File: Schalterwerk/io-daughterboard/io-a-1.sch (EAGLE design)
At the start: 34 parts, among them Q1 BSS123, Q2 BSS123, Q3 BSS123, Q4 BSS123, Q5 BSS123, Q6 BSS123, Q7 BSS123, Q8 BSS123, U1 74HC166, U2 74HC166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

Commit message: Completes board layout and routing for the daughterboard.
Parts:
- removed C2, C4: (no value), rcl:C-USC0805
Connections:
- net N$1 renamed QA
- net N$11 renamed PF
- net N$12 renamed PE
- net N$14 renamed PH
- net N$15 renamed PG
- net N$17 renamed PC
- net N$2 renamed QB
- net N$23 renamed PD
- net N$3 renamed QC
- net N$39 renamed PB
- net N$4 renamed QD
- net N$41 renamed PA
- net N$5 renamed QE
- net N$6 renamed QF
- net N$7 renamed QG
- net N$8 renamed QH
- net +12V: now also X1.6; no longer X1.1
- net +5V: no longer C2.1, C4.1
- net GND: now also X1.1; no longer C2.2, C4.2, X1.6
- net LATCH: now also X1.2; no longer X1.5
- net MISO-DN: now also X1.5; no longer X1.2
- net MOSI-DN: now also X1.4; no longer X1.3
- net SCK: now also X1.3; no longer X1.4
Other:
- moved on the sheet: C3, X1
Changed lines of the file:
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@@
 <part name="P+31" library="supply1" library_urn="urn:adsk.eagle:library:371" deviceset="+5V" device=""/>
 <part name="SJ2" library="trainlib" deviceset="SJ" device="RND2"/>
-<part name="C4" library="rcl" library_urn="urn:adsk.eagle:library:334" deviceset="C-US" device="C0805" package3d_urn="urn:adsk.eagle:package:23617/2"/>
-<part name="C2" library="rcl" library_urn="urn:adsk.eagle:library:334" deviceset="C-US" device="C0805" package3d_urn="urn:adsk.eagle:package:23617/2"/>
 <part name="U4" library="trainlib" deviceset="74*595" device="D" technology="HCT" value="74AHCT595N"/>
 <part name="SUPPLY4" library="supply2" library_urn="urn:adsk.eagle:library:372" deviceset="GND" device=""/>
@@
 <attribute name="VALUE" x="190.5" y="161.925" size="1.778" layer="96" rot="MR0"/>
 </instance>
-<instance part="X1" gate="G$1" x="236.22" y="170.18" smashed="yes" rot="R270">
-<attribute name="NAME" x="236.22" y="179.07" size="1.778" layer="95"/>
-<attribute name="VALUE" x="236.22" y="161.925" size="1.778" layer="96"/>
+<instance part="X1" gate="G$1" x="236.22" y="172.72" smashed="yes" rot="MR90">
+<attribute name="NAME" x="236.22" y="163.83" size="1.778" layer="95" rot="MR180"/>
+<attribute name="VALUE" x="236.22" y="180.975" size="1.778" layer="96" rot="MR180"/>
 </instance>
 <instance part="P+4" gate="1" x="200.66" y="182.88" smashed="yes">
@@
 <attribute name="VALUE" x="26.67" y="17.78" size="1.778" layer="96" rot="R90"/>
 </instance>
-<instance part="C4" gate="G$1" x="228.6" y="45.72" smashed="yes" rot="R90">
-<attribute name="NAME" x="232.156" y="46.355" size="1.778" layer="95"/>
-<attribute name="VALUE" x="232.791" y="46.736" size="1.778" layer="96" rot="R90"/>
-</instance>
 <instance part="U2" gate="P" x="228.6" y="83.82" smashed="yes" rot="MR270">
 <attribute name="NAME" x="226.187" y="85.725" size="1.778" layer="95" rot="MR180"/>
-</instance>
-<instance part="C2" gate="G$1" x="228.6" y="60.96" smashed="yes" rot="R90">
-<attribute name="NAME" x="232.156" y="61.595" size="1.778" layer="95"/>
-<attribute name="VALUE" x="232.791" y="61.976" size="1.778" layer="96" rot="R90"/>
 </instance>
 <instance part="U4" gate="A" x="106.68" y="35.56" smashed="yes" rot="MR0">
@@
 <attribute name="NAME" x="226.187" y="75.565" size="1.778" layer="95" rot="MR180"/>
 </instance>
-<instance part="C3" gate="G$1" x="228.6" y="53.34" smashed="yes" rot="MR270">
-<attribute name="NAME" x="231.902" y="55.753" size="1.778" layer="95" rot="MR180"/>
-<attribute name="VALUE" x="232.791" y="52.324" size="1.778" layer="96" rot="MR270"/>
-</instance>
-<instance part="SUPPLY6" gate="GND" x="241.3" y="40.64" smashed="yes" rot="MR0">
-<attribute name="VALUE" x="243.205" y="37.465" size="1.778" layer="96" rot="MR0"/>
+<instance part="C3" gate="G$1" x="228.6" y="60.96" smashed="yes" rot="MR270">
+<attribute name="NAME" x="231.902" y="63.373" size="1.778" layer="95" rot="MR180"/>
+<attribute name="VALUE" x="232.791" y="59.944" size="1.778" layer="96" rot="MR270"/>
+</instance>
+<instance part="SUPPLY6" gate="GND" x="241.3" y="53.34" smashed="yes" rot="MR0">
+<attribute name="VALUE" x="243.205" y="50.165" size="1.778" layer="96" rot="MR0"/>
 </instance>
 <instance part="R1" gate="G$1" x="55.88" y="149.86" smashed="yes" rot="R90">
@@
 </segment>
 <segment>
-<pinref part="X1" gate="G$1" pin="6"/>
-<wire x1="233.68" y1="165.1" x2="228.6" y2="165.1" width="0.1524" layer="91"/>
 <pinref part="SUPPLY2" gate="GND" pin="GND"/>
 <wire x1="228.6" y1="165.1" x2="228.6" y2="162.56" width="0.1524" layer="91"/>
+<pinref part="X1" gate="G$1" pin="1"/>
+<wire x1="228.6" y1="165.1" x2="233.68" y2="165.1" width="0.1524" layer="91"/>
 </segment>
 <segment>
@@
 <pinref part="C3" gate="G$1" pin="2"/>
 <pinref part="U3" gate="P" pin="GND"/>
-<pinref part="C4" gate="G$1" pin="2"/>
 <pinref part="U2" gate="P" pin="GND"/>
-<pinref part="C2" gate="G$1" pin="2"/>
 <pinref part="U1" gate="P" pin="GND"/>
 <pinref part="C1" gate="G$1" pin="2"/>
@@
 <wire x1="241.3" y1="73.66" x2="241.3" y2="68.58" width="0.1524" layer="91"/>
 <wire x1="241.3" y1="68.58" x2="241.3" y2="60.96" width="0.1524" layer="91"/>
-<wire x1="241.3" y1="60.96" x2="241.3" y2="53.34" width="0.1524" layer="91"/>
-<wire x1="241.3" y1="53.34" x2="241.3" y2="45.72" width="0.1524" layer="91"/>
-<wire x1="241.3" y1="45.72" x2="241.3" y2="43.18" width="0.1524" layer="91"/>
+<wire x1="241.3" y1="60.96" x2="241.3" y2="55.88" width="0.1524" layer="91"/>
 <wire x1="238.76" y1="83.82" x2="241.3" y2="83.82" width="0.1524" layer="91"/>
 <junction x="241.3" y="83.82"/>
@@
 <wire x1="233.68" y1="60.96" x2="241.3" y2="60.96" width="0.1524" layer="91"/>
 <junction x="241.3" y="60.96"/>
-<wire x1="233.68" y1="53.34" x2="241.3" y2="53.34" width="0.1524" layer="91"/>
-<junction x="241.3" y="53.34"/>
-<wire x1="233.68" y1="45.72" x2="241.3" y2="45.72" width="0.1524" layer="91"/>
-<junction x="241.3" y="45.72"/>
 </segment>
 <segment>
@@
 </segment>
 <segment>
-<wire x1="226.06" y1="175.26" x2="233.68" y2="175.26" width="0.1524" layer="91"/>
-<pinref part="X1" gate="G$1" pin="2"/>
 <label x="226.06" y="175.26" size="1.27" layer="95" rot="R180" xref="yes"/>
+<pinref part="X1" gate="G$1" pin="5"/>
+<wire x1="233.68" y1="175.26" x2="226.06" y2="175.26" width="0.1524" layer="91"/>
 </segment>
 </net>
@@
 </segment>
 <segment>
-<wire x1="233.68" y1="170.18" x2="226.06" y2="170.18" width="0.1524" layer="91"/>
 <label x="226.06" y="170.18" size="1.27" layer="95" rot="MR0" xref="yes"/>
-<pinref part="X1" gate="G$1" pin="4"/>
+<pinref part="X1" gate="G$1" pin="3"/>
+<wire x1="226.06" y1="170.18" x2="233.68" y2="170.18" width="0.1524" layer="91"/>
 </segment>
 <segment>
@@
 </segment>
 <segment>
-<wire x1="233.68" y1="167.64" x2="226.06" y2="167.64" width="0.1524" layer="91"/>
 <label x="226.06" y="167.64" size="1.27" layer="95" rot="MR0" xref="yes"/>
-<pinref part="X1" gate="G$1" pin="5"/>
+<pinref part="X1" gate="G$1" pin="2"/>
+<wire x1="226.06" y1="167.64" x2="233.68" y2="167.64" width="0.1524" layer="91"/>
 </segment>
 <segment>
@@
 </segment>
 </net>
-<net name="N$1" class="0">
+<net name="QA" class="0">
 <segment>
 <pinref part="U1" gate="A" pin="A"/>
@@
 </segment>
 </net>
-<net name="N$2" class="0">
+<net name="QB" class="0">
 <segment>
 <pinref part="U2" gate="A" pin="B"/>
@@
 </segment>
 </net>
-<net name="N$3" class="0">
+<net name="QC" class="0">
 <segment>
 <pinref part="U1" gate="A" pin="C"/>
@@
 </segment>
 </net>
-<net name="N$4" class="0">
+<net name="QD" class="0">
 <segment>
 <pinref part="U2" gate="A" pin="D"/>
@@
 </segment>
 </net>
-<net name="N$5" class="0">
+<net name="QE" class="0">
 <segment>
 <pinref part="U1" gate="A" pin="E"/>
@@
 </segment>
 </net>
-<net name="N$6" class="0">
+<net name="QF" class="0">
 <segment>
 <pinref part="U2" gate="A" pin="F"/>
@@
 </segment>
 </net>
-<net name="N$7" class="0">
+<net name="QG" class="0">
 <segment>
 <pinref part="U1" gate="A" pin="G"/>
@@
 </segment>
 </net>
-<net name="N$8" class="0">
+<net name="QH" class="0">
 <segment>
 <pinref part="U2" gate="A" pin="H"/>
@@
 <wire x1="215.9" y1="68.58" x2="226.06" y2="68.58" width="0.1524" layer="91"/>
 <junction x="215.9" y="73.66"/>
-<pinref part="C2" gate="G$1" pin="1"/>
+<junction x="215.9" y="68.58"/>
+<pinref part="C3" gate="G$1" pin="1"/>
 <wire x1="215.9" y1="68.58" x2="215.9" y2="60.96" width="0.1524" layer="91"/>
 <wire x1="215.9" y1="60.96" x2="226.06" y2="60.96" width="0.1524" layer="91"/>
-<junction x="215.9" y="68.58"/>
-<pinref part="C3" gate="G$1" pin="1"/>
-<wire x1="215.9" y1="60.96" x2="215.9" y2="53.34" width="0.1524" layer="91"/>
-<wire x1="215.9" y1="53.34" x2="226.06" y2="53.34" width="0.1524" layer="91"/>
-<junction x="215.9" y="60.96"/>
-<pinref part="C4" gate="G$1" pin="1"/>
-<wire x1="215.9" y1="53.34" x2="215.9" y2="45.72" width="0.1524" layer="91"/>
-<wire x1="215.9" y1="45.72" x2="226.06" y2="45.72" width="0.1524" layer="91"/>
-<junction x="215.9" y="53.34"/>
 </segment>
 <segment>
@@
 </segment>
 <segment>
-<pinref part="X1" gate="G$1" pin="1"/>
-<wire x1="233.68" y1="177.8" x2="228.6" y2="177.8" width="0.1524" layer="91"/>
 <pinref part="P+5" gate="1" pin="+12V"/>
 <wire x1="228.6" y1="177.8" x2="228.6" y2="180.34" width="0.1524" layer="91"/>
+<pinref part="X1" gate="G$1" pin="6"/>
+<wire x1="228.6" y1="177.8" x2="233.68" y2="177.8" width="0.1524" layer="91"/>
 </segment>
 <segment>
@@
 <net name="MOSI-DN" class="0">
 <segment>
-<pinref part="X1" gate="G$1" pin="3"/>
-<wire x1="233.68" y1="172.72" x2="226.06" y2="172.72" width="0.1524" layer="91"/>
 <label x="226.06" y="172.72" size="1.27" layer="95" rot="R180" xref="yes"/>
+<pinref part="X1" gate="G$1" pin="4"/>
+<wire x1="226.06" y1="172.72" x2="233.68" y2="172.72" width="0.1524" layer="91"/>
 </segment>
 <segment>
@@
 </segment>
 </net>
-<net name="N$12" class="0">
+<net name="PE" class="0">
 <segment>
 <pinref part="Q5" gate="G$1" pin="G"/>
@@
 </segment>
 </net>
-<net name="N$17" class="0">
+<net name="PC" class="0">
 <segment>
 <pinref part="Q3" gate="G$1" pin="G"/>
@@
 </segment>
 </net>
-<net name="N$39" class="0">
+<net name="PB" class="0">
 <segment>
 <pinref part="Q2" gate="G$1" pin="G"/>
@@
 </segment>
 </net>
-<net name="N$41" class="0">
+<net name="PA" class="0">
 <segment>
 <pinref part="Q1" gate="G$1" pin="G"/>
@@
 </segment>
 </net>
-<net name="N$11" class="0">
+<net name="PF" class="0">
 <segment>
 <pinref part="Q6" gate="G$1" pin="G"/>
@@
 </segment>
 </net>
-<net name="N$14" class="0">
+<net name="PH" class="0">
 <segment>
 <pinref part="Q8" gate="G$1" pin="G"/>
@@
 </segment>
 </net>
-<net name="N$15" class="0">
+<net name="PG" class="0">
 <segment>
 <pinref part="Q7" gate="G$1" pin="G"/>
@@
 </segment>
 </net>
-<net name="N$23" class="0">
+<net name="PD" class="0">
 <segment>
 <pinref part="Q4" gate="G$1" pin="G"/>

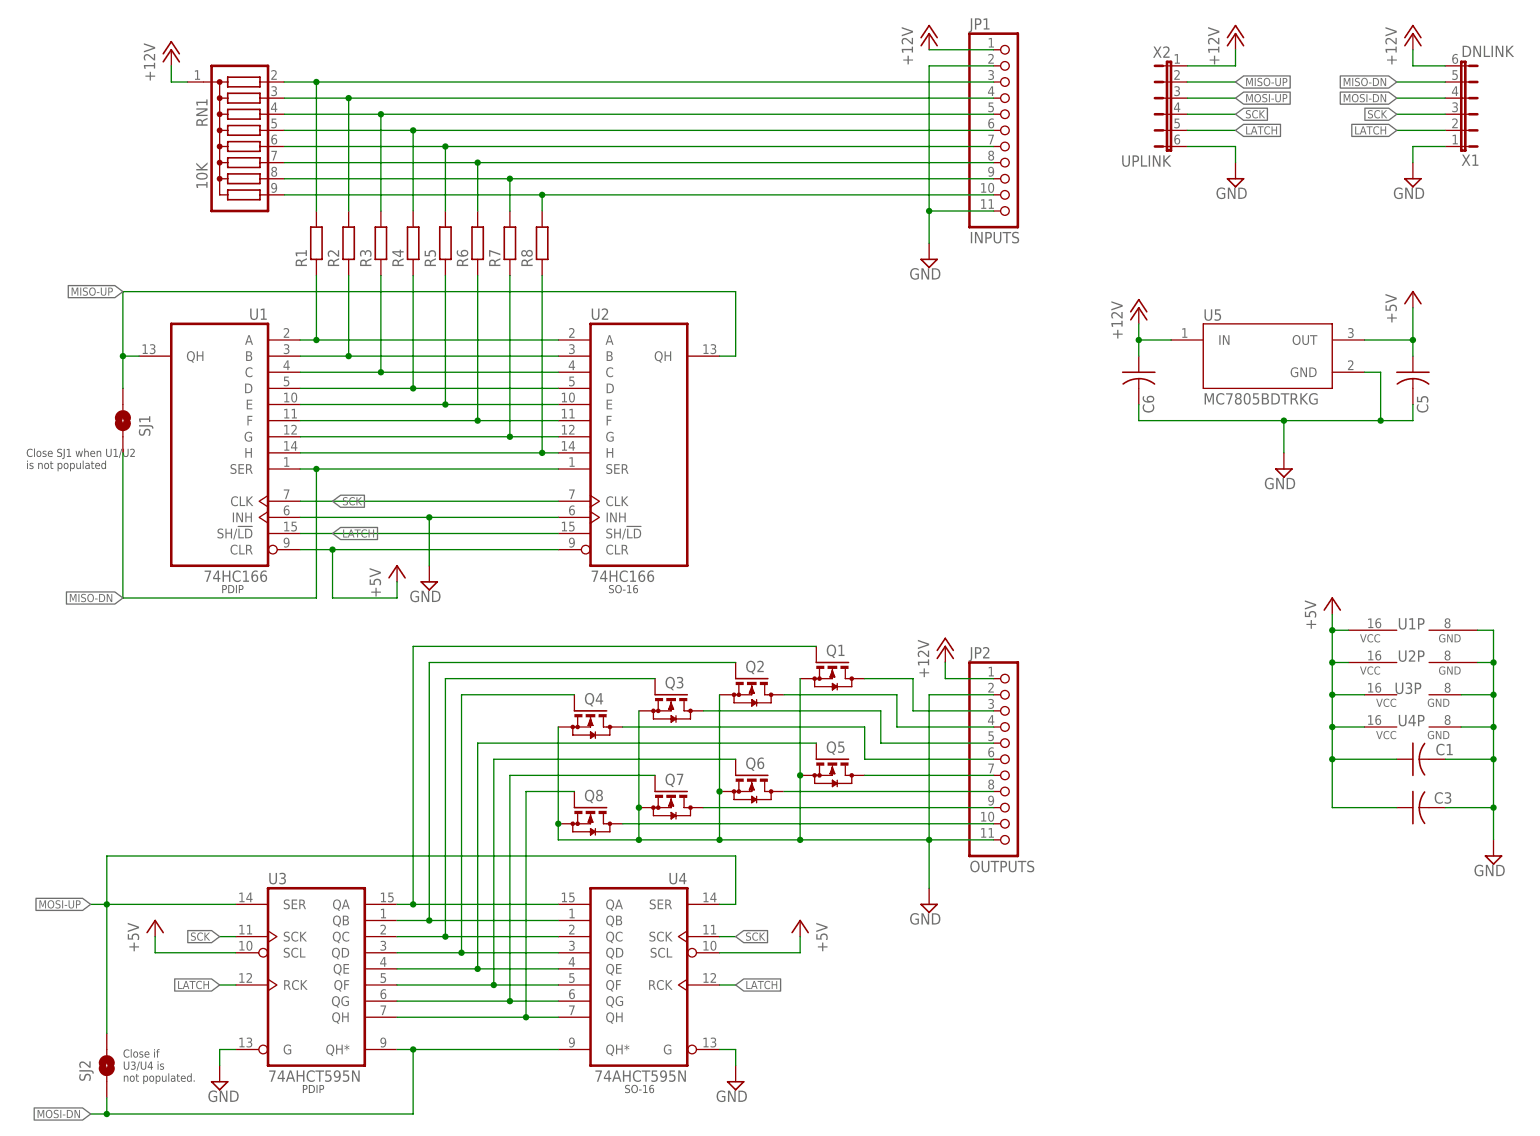
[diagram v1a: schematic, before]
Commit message: Adds molex picoblade connectors as alternative for uplink/dnlink.
Finishes layout with labels and text.
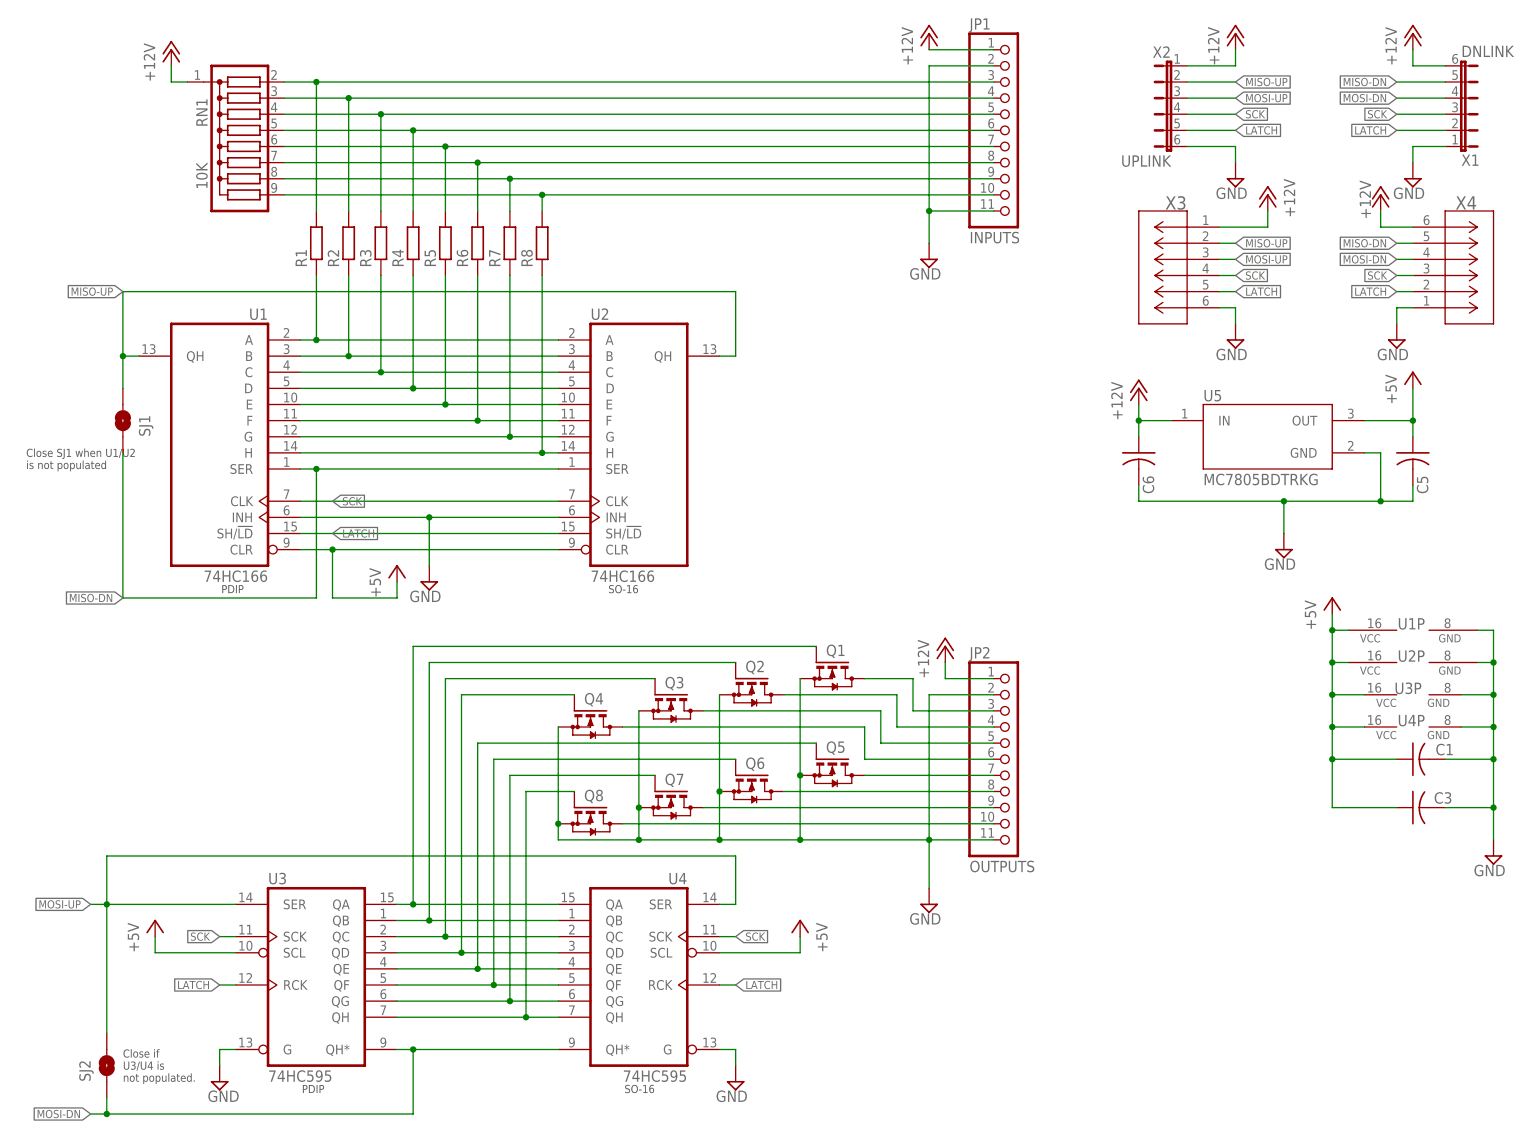
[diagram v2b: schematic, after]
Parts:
- added X3, X4: MOLEX_530470610CON_530470610_MOL, eagleparts:MOLEX_530470610CON_530470610_MOL
- U3, U4: value 74AHCT595N -> 74HC595
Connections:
- net +12V: now also X3.1, X4.6
- net GND: now also X3.6, X4.1
- net LATCH: now also X3.5, X4.2
- net MISO-DN: now also X4.5
- net MISO-UP: now also X3.2
- net MOSI-DN: now also X4.4
- net MOSI-UP: now also X3.3
- net SCK: now also X3.4, X4.3
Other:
- moved on the sheet: C5, C6, U5

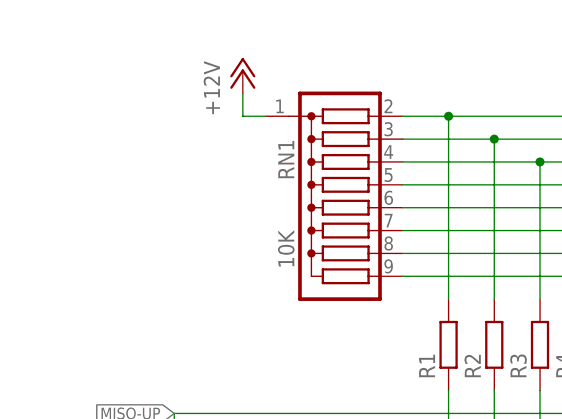
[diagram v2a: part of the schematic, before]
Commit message: Updates layout of the io daughterboard. Updates silkscreen documentation.
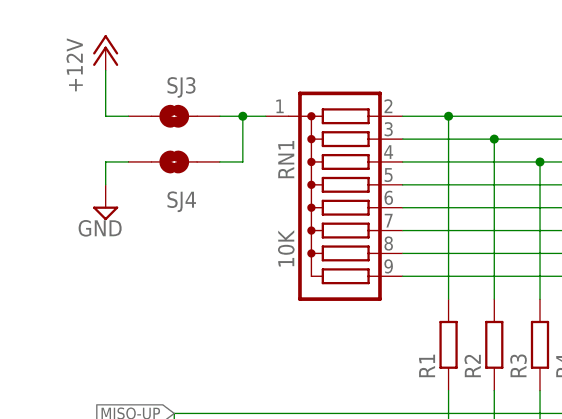
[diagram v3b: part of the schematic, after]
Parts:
- added SJ3, SJ4: (no value), trainlib:SJRND2
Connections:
- new net N$1: RN1.1, SJ3.1, SJ4.1
- net +12V: now also SJ3.2; no longer RN1.1
- net GND: now also SJ4.2
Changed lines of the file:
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@@
 <part name="P+11" library="supply1" library_urn="urn:adsk.eagle:library:371" deviceset="+12V" device=""/>
 <part name="P+12" library="supply1" library_urn="urn:adsk.eagle:library:371" deviceset="+12V" device=""/>
+<part name="SJ3" library="trainlib" deviceset="SJ" device="RND2"/>
+<part name="SJ4" library="trainlib" deviceset="SJ" device="RND2"/>
+<part name="SUPPLY10" library="supply2" library_urn="urn:adsk.eagle:library:372" deviceset="GND" device=""/>
 </parts>
 <sheets>
@@
 <attribute name="VALUE" x="149.86" y="177.8" size="1.778" layer="96" rot="R90"/>
 </instance>
-<instance part="P+8" gate="1" x="33.02" y="180.34" smashed="yes">
-<attribute name="VALUE" x="30.48" y="175.26" size="1.778" layer="96" rot="R90"/>
+<instance part="P+8" gate="1" x="17.78" y="182.88" smashed="yes">
+<attribute name="VALUE" x="15.24" y="177.8" size="1.778" layer="96" rot="R90"/>
 </instance>
 <instance part="U5" gate="G$1" x="205.74" y="119.38" smashed="yes">
@@
 <instance part="P+12" gate="1" x="223.52" y="157.48" smashed="yes">
 <attribute name="VALUE" x="220.218" y="159.766" size="1.778" layer="96" rot="R270"/>
+</instance>
+<instance part="SJ3" gate="1" x="25.4" y="175.26" smashed="yes" rot="MR0">
+<attribute name="NAME" x="27.94" y="177.8" size="1.778" layer="95" rot="MR0"/>
+<attribute name="VALUE" x="27.94" y="171.45" size="1.778" layer="96" rot="MR0"/>
+</instance>
+<instance part="SJ4" gate="1" x="25.4" y="170.18" smashed="yes" rot="MR0">
+<attribute name="NAME" x="27.94" y="165.1" size="1.778" layer="95" rot="MR0"/>
+<attribute name="VALUE" x="27.94" y="166.37" size="1.778" layer="96" rot="MR0"/>
+</instance>
+<instance part="SUPPLY10" gate="GND" x="17.78" y="165.1" smashed="yes" rot="MR0">
+<attribute name="VALUE" x="19.685" y="161.925" size="1.778" layer="96" rot="MR0"/>
 </instance>
 </instances>
@@
 <wire x1="226.06" y1="139.7" x2="226.06" y2="137.16" width="0.1524" layer="91"/>
 </segment>
+<segment>
+<pinref part="SUPPLY10" gate="GND" pin="GND"/>
+<wire x1="17.78" y1="170.18" x2="17.78" y2="167.64" width="0.1524" layer="91"/>
+<pinref part="SJ4" gate="1" pin="2"/>
+<wire x1="17.78" y1="170.18" x2="20.32" y2="170.18" width="0.1524" layer="91"/>
+</segment>
 </net>
 <net name="MISO-DN" class="0">
@@
 </segment>
 <segment>
-<pinref part="RN1" gate="G$1" pin="1"/>
-<wire x1="35.56" y1="175.26" x2="33.02" y2="175.26" width="0.1524" layer="91"/>
 <pinref part="P+8" gate="1" pin="+12V"/>
-<wire x1="33.02" y1="175.26" x2="33.02" y2="177.8" width="0.1524" layer="91"/>
+<wire x1="17.78" y1="175.26" x2="17.78" y2="180.34" width="0.1524" layer="91"/>
+<pinref part="SJ3" gate="1" pin="2"/>
+<wire x1="17.78" y1="175.26" x2="20.32" y2="175.26" width="0.1524" layer="91"/>
 </segment>
 <segment>
@@
 </segment>
 </net>
+<net name="N$1" class="0">
+<segment>
+<pinref part="RN1" gate="G$1" pin="1"/>
+<wire x1="35.56" y1="175.26" x2="33.02" y2="175.26" width="0.1524" layer="91"/>
+<wire x1="33.02" y1="175.26" x2="33.02" y2="170.18" width="0.1524" layer="91"/>
+<pinref part="SJ4" gate="1" pin="1"/>
+<wire x1="33.02" y1="170.18" x2="30.48" y2="170.18" width="0.1524" layer="91"/>
+<pinref part="SJ3" gate="1" pin="1"/>
+<wire x1="33.02" y1="175.26" x2="30.48" y2="175.26" width="0.1524" layer="91"/>
+<junction x="33.02" y="175.26"/>
+</segment>
+</net>
